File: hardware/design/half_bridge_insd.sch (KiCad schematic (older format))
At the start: 14 parts

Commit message: Added pullup resistor for THWn. Fixed some not connected parts warnings.
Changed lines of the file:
@@
 AR Path="/56BA2E2B/55DF8D4F" Ref="Cboot5"  Part="1"
 AR Path="/56BA5F82/55DF8D4F" Ref="Cboot6"  Part="1"
-F 0 "Cboot1" V 6647 3700 50  0000 C CNN
+F 0 "Cboot6" V 6647 3700 50  0000 C CNN
 F 1 "0.47uF" V 6739 3700 50  0000 C CNN
 F 2 "Capacitors_SMD:C_0603_HandSoldering" H 6938 3550 30  0001 C CNN
@@
 AR Path="/56BA2E2B/55DF8D84" Ref="CDrGate5"  Part="1"
 AR Path="/56BA5F82/55DF8D84" Ref="CDrGate6"  Part="1"
-F 0 "CDrGate1" H 5065 2946 50  0000 L CNN
+F 0 "CDrGate6" H 5065 2946 50  0000 L CNN
 F 1 "0.47uF" H 5065 2854 50  0000 L CNN
 F 2 "Capacitors_SMD:C_0603_HandSoldering" H 4988 2750 30  0001 C CNN
@@
 AR Path="/56BA2E2B/56984538" Ref="Usens5"  Part="1"
 AR Path="/56BA5F82/56984538" Ref="Usens6"  Part="1"
-F 0 "Usens1" V 7797 2922 60  0000 R CNN
+F 0 "Usens6" V 7797 2922 60  0000 R CNN
 F 1 "ACS711" V 7903 2922 60  0000 R CNN
 F 2 "Allegro:QFN-12-1EX_3x3mm_Pitch0.5mm" V 7956 2922 60  0001 R CNN
@@
 AR Path="/56BA2E2B/56A19C85" Ref="UDrmos5"  Part="1"
 AR Path="/56BA5F82/56A19C85" Ref="UDrmos6"  Part="1"
-F 0 "UDrmos1" H 5650 5071 50  0000 C CNN
+F 0 "UDrmos6" H 5650 5071 50  0000 C CNN
 F 1 "DrMOS_SiC632A" H 5650 4979 50  0000 C CNN
 F 2 "DrMOS:MLP55-31L" H 5650 4887 50  0000 C CNN
@@
 AR Path="/56BA2E2B/56A2CDC4" Ref="CDrLogic5"  Part="1"
 AR Path="/56BA5F82/56A2CDC4" Ref="CDrLogic6"  Part="1"
-F 0 "CDrLogic1" H 4415 3446 50  0000 L CNN
+F 0 "CDrLogic6" H 4415 3446 50  0000 L CNN
 F 1 "2.2uF" H 4415 3354 50  0000 L CNN
 F 2 "Capacitors_SMD:C_0603" H 4338 3250 30  0001 C CNN
@@
 AR Path="/56BA2E2B/56A2D0BC" Ref="RDrLogic5"  Part="1"
 AR Path="/56BA5F82/56A2D0BC" Ref="RDrLogic6"  Part="1"
-F 0 "RDrLogic1" H 4370 2946 50  0000 L CNN
+F 0 "RDrLogic6" H 4370 2946 50  0000 L CNN
 F 1 "R" H 4370 2854 50  0000 L CNN
 F 2 "Resistors_SMD:R_0603" V 4230 2900 50  0001 C CNN
@@
 AR Path="/56BA2E2B/56A2FD69" Ref="Rhsens5"  Part="1"
 AR Path="/56BA5F82/56A2FD69" Ref="Rhsens6"  Part="1"
-F 0 "Rhsens1" H 7520 4346 50  0000 L CNN
+F 0 "Rhsens6" H 7520 4346 50  0000 L CNN
 F 1 "10k" H 7520 4254 50  0000 L CNN
 F 2 "Capacitors_SMD:C_0603_HandSoldering" V 7380 4300 50  0001 C CNN
@@
 AR Path="/56BA2E2B/56A2FEAC" Ref="Rlsens5"  Part="1"
 AR Path="/56BA5F82/56A2FEAC" Ref="Rlsens6"  Part="1"
-F 0 "Rlsens1" H 7520 4746 50  0000 L CNN
+F 0 "Rlsens6" H 7520 4746 50  0000 L CNN
 F 1 "2k2" H 7520 4654 50  0000 L CNN
 F 2 "Resistors_SMD:R_0402" V 7380 4700 50  0001 C CNN
@@
 AR Path="/56BA2E2B/56A3225A" Ref="Rcfilt5"  Part="1"
 AR Path="/56BA5F82/56A3225A" Ref="Rcfilt6"  Part="1"
-F 0 "Rcfilt1" H 8420 2846 50  0000 L CNN
+F 0 "Rcfilt6" H 8420 2846 50  0000 L CNN
 F 1 "R" H 8420 2754 50  0000 L CNN
 F 2 "Resistors_SMD:R_0402" V 8280 2800 50  0001 C CNN
@@
 AR Path="/56BA2E2B/56A3233B" Ref="Ccfilt5"  Part="1"
 AR Path="/56BA5F82/56A3233B" Ref="Ccfilt6"  Part="1"
-F 0 "Ccfilt1" H 8165 2846 50  0000 L CNN
+F 0 "Ccfilt6" H 8165 2846 50  0000 L CNN
 F 1 "C" H 8165 2754 50  0000 L CNN
 F 2 "Capacitors_SMD:C_0402" H 8088 2650 50  0001 C CNN
@@
 AR Path="/56BA2E2B/56A69B0E" Ref="CDrHV5"  Part="1"
 AR Path="/56BA5F82/56A69B0E" Ref="CDrHV6"  Part="1"
-F 0 "CDrHV1" H 5865 1246 50  0000 L CNN
+F 0 "CDrHV6" H 5865 1246 50  0000 L CNN
 F 1 "10u" H 5865 1154 50  0000 L CNN
 F 2 "Capacitors_SMD:C_1206" H 5788 1050 50  0001 C CNN
@@
 AR Path="/56BA2E2B/56AF6D20" Ref="CDrHVs5"  Part="1"
 AR Path="/56BA5F82/56AF6D20" Ref="CDrHVs6"  Part="1"
-F 0 "CDrHVs1" H 5315 1246 50  0000 L CNN
+F 0 "CDrHVs6" H 5315 1246 50  0000 L CNN
 F 1 "0.47u" H 5315 1154 50  0000 L CNN
 F 2 "Capacitors_SMD:C_0603" H 5315 1108 50  0001 L CNN
@@
 AR Path="/56BA2E2B/56B30AD6" Ref="PMotor5"  Part="1"
 AR Path="/56BA5F82/56B30AD6" Ref="PMotor6"  Part="1"
-F 0 "PMotor1" H 9177 4106 60  0000 L CNN
+F 0 "PMotor6" H 9177 4106 60  0000 L CNN
 F 1 "PAD_SMD" H 9177 4000 60  0000 L CNN
 F 2 "CRF1:1PAD_4x5mm" H 9177 3894 60  0000 L CNN
@@
 AR Path="/56BA2E2B/56B897AB" Ref="Csens5"  Part="1"
 AR Path="/56BA5F82/56B897AB" Ref="Csens6"  Part="1"
-F 0 "Csens1" H 6965 2142 50  0000 L CNN
+F 0 "Csens6" H 6965 2142 50  0000 L CNN
 F 1 "0.47u" H 6965 2050 50  0000 L CNN
 F 2 "Capacitors_SMD:C_0603" H 6965 1958 50  0000 L CNN

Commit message: Guessing current filter values ;-)
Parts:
- Ccfilt1: value C -> 0.5n
- Rcfilt1: value R -> 20k
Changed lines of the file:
@@
 LIBS:memory
 LIBS:xilinx
-LIBS:special
 LIBS:microcontrollers
 LIBS:dsp
@@
 AR Path="/56BA2E2B/55DF8D4F" Ref="Cboot5"  Part="1"
 AR Path="/56BA5F82/55DF8D4F" Ref="Cboot6"  Part="1"
-F 0 "Cboot6" V 6647 3700 50  0000 C CNN
+F 0 "Cboot1" V 6647 3700 50  0000 C CNN
 F 1 "0.47uF" V 6739 3700 50  0000 C CNN
 F 2 "Capacitors_SMD:C_0603_HandSoldering" H 6938 3550 30  0001 C CNN
@@
 AR Path="/56BA2E2B/55DF8D84" Ref="CDrGate5"  Part="1"
 AR Path="/56BA5F82/55DF8D84" Ref="CDrGate6"  Part="1"
-F 0 "CDrGate6" H 5065 2946 50  0000 L CNN
+F 0 "CDrGate1" H 5065 2946 50  0000 L CNN
 F 1 "0.47uF" H 5065 2854 50  0000 L CNN
 F 2 "Capacitors_SMD:C_0603_HandSoldering" H 4988 2750 30  0001 C CNN
@@
 AR Path="/56BA2E2B/56984538" Ref="Usens5"  Part="1"
 AR Path="/56BA5F82/56984538" Ref="Usens6"  Part="1"
-F 0 "Usens6" V 7797 2922 60  0000 R CNN
+F 0 "Usens1" V 7797 2922 60  0000 R CNN
 F 1 "ACS711" V 7903 2922 60  0000 R CNN
 F 2 "Allegro:QFN-12-1EX_3x3mm_Pitch0.5mm" V 7956 2922 60  0001 R CNN
@@
 AR Path="/56BA2E2B/56A19C85" Ref="UDrmos5"  Part="1"
 AR Path="/56BA5F82/56A19C85" Ref="UDrmos6"  Part="1"
-F 0 "UDrmos6" H 5650 5071 50  0000 C CNN
+F 0 "UDrmos1" H 5650 5071 50  0000 C CNN
 F 1 "DrMOS_SiC632A" H 5650 4979 50  0000 C CNN
 F 2 "DrMOS:MLP55-31L" H 5650 4887 50  0000 C CNN
@@
 AR Path="/56BA2E2B/56A2AE4F" Ref="#PWR076"  Part="1"
 AR Path="/56BA5F82/56A2AE4F" Ref="#PWR089"  Part="1"
-F 0 "#PWR089" H 5750 4850 50  0001 C CNN
+F 0 "#PWR014" H 5750 4850 50  0001 C CNN
 F 1 "GNDPWR" H 5750 4900 50  0000 C CNN
 F 2 "" H 5750 5000 50  0000 C CNN
@@
 AR Path="/56BA2E2B/56A2B769" Ref="#PWR077"  Part="1"
 AR Path="/56BA5F82/56A2B769" Ref="#PWR090"  Part="1"
-F 0 "#PWR090" H 5200 4750 50  0001 C CNN
+F 0 "#PWR015" H 5200 4750 50  0001 C CNN
 F 1 "GND" H 5208 4826 50  0000 C CNN
 F 2 "" H 5200 5000 50  0000 C CNN
@@
 AR Path="/56BA2E2B/56A2BBEE" Ref="#PWR078"  Part="1"
 AR Path="/56BA5F82/56A2BBEE" Ref="#PWR091"  Part="1"
-F 0 "#PWR091" H 4950 3000 50  0001 C CNN
+F 0 "#PWR016" H 4950 3000 50  0001 C CNN
 F 1 "GNDPWR" H 4957 3275 50  0000 C CNN
 F 2 "" H 4950 3150 50  0000 C CNN
@@
 AR Path="/56BA2E2B/56A2CDC4" Ref="CDrLogic5"  Part="1"
 AR Path="/56BA5F82/56A2CDC4" Ref="CDrLogic6"  Part="1"
-F 0 "CDrLogic6" H 4415 3446 50  0000 L CNN
+F 0 "CDrLogic1" H 4415 3446 50  0000 L CNN
 F 1 "2.2uF" H 4415 3354 50  0000 L CNN
 F 2 "Capacitors_SMD:C_0603" H 4338 3250 30  0001 C CNN
@@
 AR Path="/56BA2E2B/56A2CDEC" Ref="#PWR079"  Part="1"
 AR Path="/56BA5F82/56A2CDEC" Ref="#PWR092"  Part="1"
-F 0 "#PWR092" H 4300 3300 50  0001 C CNN
+F 0 "#PWR017" H 4300 3300 50  0001 C CNN
 F 1 "GND" H 4308 3376 50  0000 C CNN
 F 2 "" H 4300 3550 50  0000 C CNN
@@
 AR Path="/56BA2E2B/56A2CF9B" Ref="#PWR080"  Part="1"
 AR Path="/56BA5F82/56A2CF9B" Ref="#PWR093"  Part="1"
-F 0 "#PWR093" H 4300 2500 50  0001 C CNN
+F 0 "#PWR018" H 4300 2500 50  0001 C CNN
 F 1 "+5V" H 4318 2824 50  0000 C CNN
 F 2 "" H 4300 2650 50  0000 C CNN
@@
 AR Path="/56BA2E2B/56A2D0BC" Ref="RDrLogic5"  Part="1"
 AR Path="/56BA5F82/56A2D0BC" Ref="RDrLogic6"  Part="1"
-F 0 "RDrLogic6" H 4370 2946 50  0000 L CNN
+F 0 "RDrLogic1" H 4370 2946 50  0000 L CNN
 F 1 "R" H 4370 2854 50  0000 L CNN
 F 2 "Resistors_SMD:R_0603" V 4230 2900 50  0001 C CNN
@@
 AR Path="/56BA2E2B/56A2EFF6" Ref="#PWR081"  Part="1"
 AR Path="/56BA5F82/56A2EFF6" Ref="#PWR094"  Part="1"
-F 0 "#PWR094" H 8550 2800 50  0001 C CNN
+F 0 "#PWR019" H 8550 2800 50  0001 C CNN
 F 1 "GND" H 8558 2876 50  0000 C CNN
 F 2 "" H 8550 3050 50  0000 C CNN
@@
 AR Path="/56BA2E2B/56A2FD69" Ref="Rhsens5"  Part="1"
 AR Path="/56BA5F82/56A2FD69" Ref="Rhsens6"  Part="1"
-F 0 "Rhsens6" H 7520 4346 50  0000 L CNN
+F 0 "Rhsens1" H 7520 4346 50  0000 L CNN
 F 1 "10k" H 7520 4254 50  0000 L CNN
 F 2 "Capacitors_SMD:C_0603_HandSoldering" V 7380 4300 50  0001 C CNN
@@
 AR Path="/56BA2E2B/56A2FEAC" Ref="Rlsens5"  Part="1"
 AR Path="/56BA5F82/56A2FEAC" Ref="Rlsens6"  Part="1"
-F 0 "Rlsens6" H 7520 4746 50  0000 L CNN
+F 0 "Rlsens1" H 7520 4746 50  0000 L CNN
 F 1 "2k2" H 7520 4654 50  0000 L CNN
 F 2 "Resistors_SMD:R_0402" V 7380 4700 50  0001 C CNN
@@
 AR Path="/56BA2E2B/56A30067" Ref="#PWR082"  Part="1"
 AR Path="/56BA5F82/56A30067" Ref="#PWR095"  Part="1"
-F 0 "#PWR095" H 7450 4700 50  0001 C CNN
+F 0 "#PWR020" H 7450 4700 50  0001 C CNN
 F 1 "GND" H 7458 4776 50  0000 C CNN
 F 2 "" H 7450 4950 50  0000 C CNN
@@
 AR Path="/56BA2E2B/56A31D68" Ref="#PWR083"  Part="1"
 AR Path="/56BA5F82/56A31D68" Ref="#PWR096"  Part="1"
-F 0 "#PWR096" H 6050 2850 50  0001 C CNN
+F 0 "#PWR021" H 6050 2850 50  0001 C CNN
 F 1 "+24V" H 6068 3174 50  0000 C CNN
 F 2 "" H 6050 3000 50  0000 C CNN
@@
 AR Path="/56BA2E2B/56A32138" Ref="#PWR084"  Part="1"
 AR Path="/56BA5F82/56A32138" Ref="#PWR097"  Part="1"
-F 0 "#PWR097" H 7350 2500 50  0001 C CNN
+F 0 "#PWR022" H 7350 2500 50  0001 C CNN
 F 1 "+3.3V" H 7368 2824 50  0000 C CNN
 F 2 "" H 7350 2650 50  0000 C CNN
@@
 AR Path="/56BA2E2B/56A3225A" Ref="Rcfilt5"  Part="1"
 AR Path="/56BA5F82/56A3225A" Ref="Rcfilt6"  Part="1"
-F 0 "Rcfilt6" H 8420 2846 50  0000 L CNN
-F 1 "R" H 8420 2754 50  0000 L CNN
+F 0 "Rcfilt1" H 8420 2846 50  0000 L CNN
+F 1 "20k" H 8420 2754 50  0000 L CNN
 F 2 "Resistors_SMD:R_0402" V 8280 2800 50  0001 C CNN
 F 3 "" H 8350 2800 50  0000 C CNN
@@
 AR Path="/56BA2E2B/56A3233B" Ref="Ccfilt5"  Part="1"
 AR Path="/56BA5F82/56A3233B" Ref="Ccfilt6"  Part="1"
-F 0 "Ccfilt6" H 8165 2846 50  0000 L CNN
-F 1 "C" H 8165 2754 50  0000 L CNN
+F 0 "Ccfilt1" H 8165 2846 50  0000 L CNN
+F 1 "0.5n" H 8165 2754 50  0000 L CNN
 F 2 "Capacitors_SMD:C_0402" H 8088 2650 50  0001 C CNN
 F 3 "" H 8050 2800 50  0000 C CNN
@@
 AR Path="/56BA2E2B/56A69AD2" Ref="#PWR085"  Part="1"
 AR Path="/56BA5F82/56A69AD2" Ref="#PWR098"  Part="1"
-F 0 "#PWR098" H 5750 800 50  0001 C CNN
+F 0 "#PWR023" H 5750 800 50  0001 C CNN
 F 1 "+24V" H 5768 1124 50  0000 C CNN
 F 2 "" H 5750 950 50  0000 C CNN
@@
 AR Path="/56BA2E2B/56A69B0E" Ref="CDrHV5"  Part="1"
 AR Path="/56BA5F82/56A69B0E" Ref="CDrHV6"  Part="1"
-F 0 "CDrHV6" H 5865 1246 50  0000 L CNN
+F 0 "CDrHV1" H 5865 1246 50  0000 L CNN
 F 1 "10u" H 5865 1154 50  0000 L CNN
 F 2 "Capacitors_SMD:C_1206" H 5788 1050 50  0001 C CNN
@@
 AR Path="/56BA2E2B/56A69BA7" Ref="#PWR086"  Part="1"
 AR Path="/56BA5F82/56A69BA7" Ref="#PWR099"  Part="1"
-F 0 "#PWR099" H 5750 1300 50  0001 C CNN
+F 0 "#PWR024" H 5750 1300 50  0001 C CNN
 F 1 "GNDPWR" H 5757 1575 50  0000 C CNN
 F 2 "" H 5750 1450 50  0000 C CNN
@@
 AR Path="/56BA2E2B/56AF6D20" Ref="CDrHVs5"  Part="1"
 AR Path="/56BA5F82/56AF6D20" Ref="CDrHVs6"  Part="1"
-F 0 "CDrHVs6" H 5315 1246 50  0000 L CNN
+F 0 "CDrHVs1" H 5315 1246 50  0000 L CNN
 F 1 "0.47u" H 5315 1154 50  0000 L CNN
 F 2 "Capacitors_SMD:C_0603" H 5315 1108 50  0001 L CNN
@@
 AR Path="/56BA2E2B/56B30AD6" Ref="PMotor5"  Part="1"
 AR Path="/56BA5F82/56B30AD6" Ref="PMotor6"  Part="1"
-F 0 "PMotor6" H 9177 4106 60  0000 L CNN
+F 0 "PMotor1" H 9177 4106 60  0000 L CNN
 F 1 "PAD_SMD" H 9177 4000 60  0000 L CNN
 F 2 "CRF1:1PAD_4x5mm" H 9177 3894 60  0000 L CNN
@@
 AR Path="/56BA2E2B/56B897AB" Ref="Csens5"  Part="1"
 AR Path="/56BA5F82/56B897AB" Ref="Csens6"  Part="1"
-F 0 "Csens6" H 6965 2142 50  0000 L CNN
+F 0 "Csens1" H 6965 2142 50  0000 L CNN
 F 1 "0.47u" H 6965 2050 50  0000 L CNN
 F 2 "Capacitors_SMD:C_0603" H 6965 1958 50  0000 L CNN
@@
 AR Path="/56BA2E2B/56B89931" Ref="#PWR087"  Part="1"
 AR Path="/56BA5F82/56B89931" Ref="#PWR0100"  Part="1"
-F 0 "#PWR0100" H 6850 1950 50  0001 C CNN
+F 0 "#PWR025" H 6850 1950 50  0001 C CNN
 F 1 "GND" H 6858 2026 50  0000 C CNN
 F 2 "" H 6850 2200 50  0000 C CNN
@@
 AR Path="/56BA2E2B/56B89961" Ref="#PWR088"  Part="1"
 AR Path="/56BA5F82/56B89961" Ref="#PWR0101"  Part="1"
-F 0 "#PWR0101" H 6850 1750 50  0001 C CNN
+F 0 "#PWR026" H 6850 1750 50  0001 C CNN
 F 1 "+3.3V" H 6868 2074 50  0000 C CNN
 F 2 "" H 6850 1900 50  0000 C CNN

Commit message: Added a few caps on the back next to the DrMOS
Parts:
- added CDrHV1back1: 4.7u, Capacitors_SMD:C_1206, symbol C
- added CDrHV2back1: 4.7u, Capacitors_SMD:C_1206_HandSoldering, symbol C
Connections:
- net +24V: now also CDrHV1back1.1, CDrHV2back1.1
- net GNDPWR: now also CDrHV1back1.2, CDrHV2back1.2

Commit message: Added pads PVsensx for the application of alterate voltage sensing probes.
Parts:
- added PVSens1: PAD_SMD, Pads:PAD_SMD_1x1, symbol PAD_SMD
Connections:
- net at PMotor1.1 (PAD), Rhsens1.1, Usens1.3 (IP-)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: now also PVSens1.1 (PAD)
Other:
- note added: "SENSV = Rlsens / (Rlsens+Rhsens)\nMust be below 4V to protect the input pin of STM32F4.\nIs 3.8V for Rl=2k2 and Rh=10k\n\nNote:\nRlsens is placed close to the controller and\nRhsens at the pad. Having load at the wire would make\nit less susceptible to noise.\n\nPad PVSens is for alternate motor voltage sensing\nthan the actual phase"
- note removed: "SENSV = Rlsens / (Rlsens+Rhsens)\nMust be below 4V to protect the input pin of STM32F4.\nIs 3.8V for Rl=2k2 and Rh=10k\n\nNote:\nThink about placing Rlsens close to the controller and\nRhsens at the pad. Having load at the wire would make\nit less susceptible to noise."

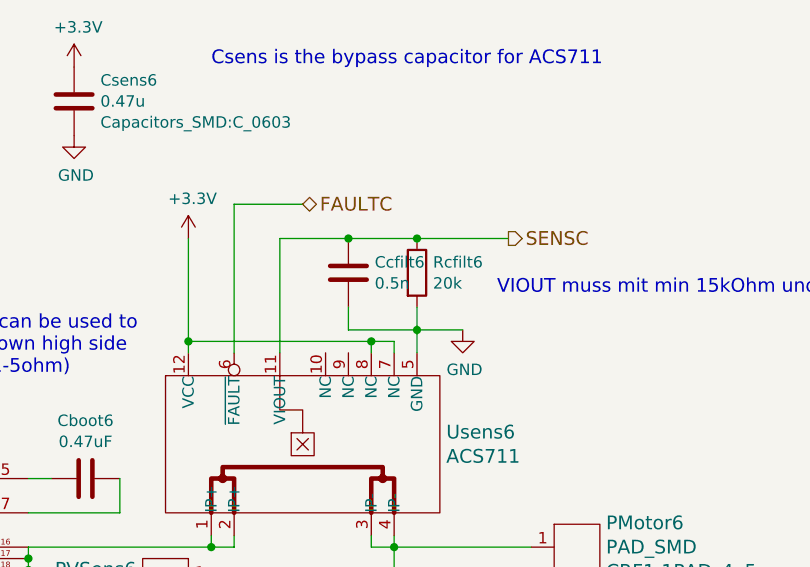
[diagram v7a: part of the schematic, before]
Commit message: Added pads for emergency bootloader execution.
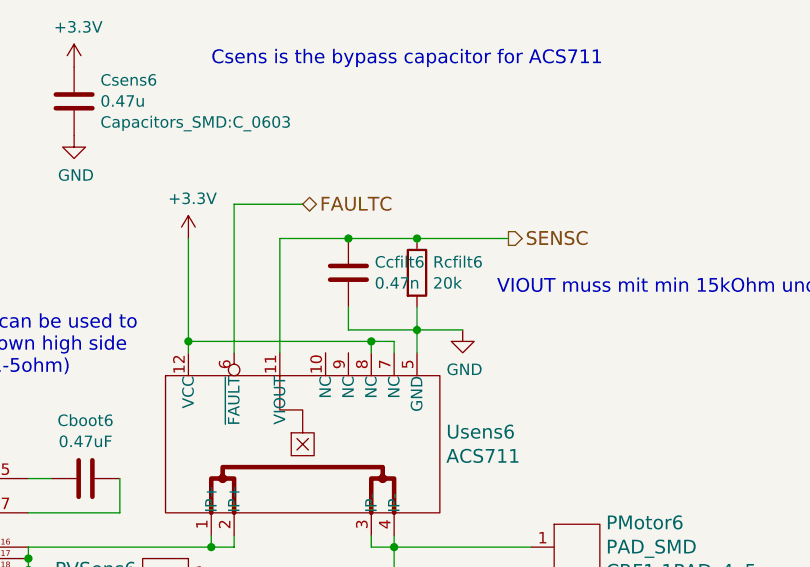
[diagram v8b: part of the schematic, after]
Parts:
- Ccfilt1: value 0.5n -> 0.47n
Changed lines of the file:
@@
 $Descr A4 11693 8268
 encoding utf-8
-Sheet 6 11
+Sheet 3 11
 Title "DrMOS power stage"
 Date "2016-01-22"
@@
 AR Path="/56BA5F82/56A3233B" Ref="Ccfilt6"  Part="1"
 F 0 "Ccfilt6" H 8165 2846 50  0000 L CNN
-F 1 "0.5n" H 8165 2754 50  0000 L CNN
+F 1 "0.47n" H 8165 2754 50  0000 L CNN
 F 2 "Capacitors_SMD:C_0402" H 8088 2650 50  0001 C CNN
 F 3 "" H 8050 2800 50  0000 C CNN
